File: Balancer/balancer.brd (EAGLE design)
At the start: 139.7 x 325.1 mm, 322 parts, among them Q1 BSS123W, Q10A SIR882DP-T1-GE3, Q10B SIS468DN-T1-GE3, Q11A SIR882DP-T1-GE3, Q11B SIS468DN-T1-GE3, Q12A SIR882DP-T1-GE3, Q12B SIS468DN-T1-GE3, Q1A8 SIR882DP-T1-GE3, Q1B8 SIS468DN-T1-GE3, Q2 BSS123W, Q3A SIR882DP-T1-GE3, Q3B SIS468DN-T1-GE3, Q4 MMBT3906LT1G, Q4A SIR882DP-T1-GE3, Q4B SIS468DN-T1-GE3, Q5 FDN5618P, Q5A SIR882DP-T1-GE3, Q5B SIS468DN-T1-GE3, Q6 CMPT3904E_TR_PBFREE, Q6A SIR882DP-T1-GE3, Q6B SIS468DN-T1-GE3, Q9A SIR882DP-T1-GE3, Q9B SIS468DN-T1-GE3, T10 750312504, T11 750312504, T12 750312504, T3 750312504, T4 750312504, T5 750312504, T6 750312504, T8 750312504, T9 750312504, U1 LTC3300ILXE-1PBF, U2 LTC3300ILXE-1PBF

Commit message: merged C8 and C6
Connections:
- removed net C8: C9A.2, C9B.2, C9G.2, D9C.A, D9E.P$2, D9E.P$3, R8K.1, R9J.1, RS9A.1
- net C6: now also C9A.2, C9B.2, C9G.2, D9C.A, D9E.P$2, D9E.P$3, R8K.1, R9J.1, RS9A.1
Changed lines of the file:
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@@
 <layers>
 <layer number="1" name="Top" color="4" fill="1" visible="yes" active="yes"/>
-<layer number="2" name="Route2" color="16" fill="1" visible="yes" active="yes"/>
+<layer number="2" name="Route2" color="16" fill="1" visible="no" active="yes"/>
 <layer number="3" name="Route3" color="17" fill="1" visible="no" active="no"/>
 <layer number="4" name="Route4" color="18" fill="1" visible="no" active="no"/>
@@
 <vertex x="95.758" y="258.191"/>
 </polygon>
+<contactref element="D9E" pad="P$2"/>
+<contactref element="D9E" pad="P$3"/>
+<contactref element="C9B" pad="2"/>
+<contactref element="C9A" pad="2"/>
+<contactref element="D9C" pad="A"/>
+<contactref element="C9G" pad="2"/>
+<contactref element="RS9A" pad="1"/>
+<contactref element="R9J" pad="1"/>
+<contactref element="R8K" pad="1"/>
 <wire x1="13.462" y1="244.21" x2="13.462" y2="240.4" width="0" layer="19" extent="1-1"/>
 <wire x1="17.907" y1="245.48" x2="13.462" y2="244.21" width="0" layer="19" extent="1-1"/>
@@
 <wire x1="30.75" y1="231.14" x2="26.46" y2="233.36" width="0" layer="19" extent="16-16"/>
 <wire x1="36.7" y1="232.41" x2="30.75" y2="231.14" width="0" layer="19" extent="16-16"/>
-<wire x1="42.418" y1="234.05" x2="36.7" y2="232.41" width="0" layer="19" extent="1-16"/>
+<wire x1="36.957" y1="233.669" x2="36.7" y2="232.41" width="0" layer="19" extent="1-16"/>
+<wire x1="39.116" y1="233.261" x2="36.957" y2="233.669" width="0" layer="19" extent="1-1"/>
+<wire x1="42.418" y1="234.05" x2="39.116" y2="233.261" width="0" layer="19" extent="1-1"/>
 <wire x1="15.24" y1="233.31" x2="13.462" y2="240.4" width="0" layer="19" extent="1-1"/>
 <wire x1="17.78" y1="233.31" x2="15.24" y2="233.31" width="0" layer="19" extent="1-1"/>
@@
 <wire x1="21.59" y1="256.67" x2="14.34" y2="252.73" width="0" layer="19" extent="1-1"/>
 <wire x1="44.32" y1="246.38" x2="42.418" y2="234.05" width="0" layer="19" extent="1-16"/>
+<wire x1="62.23" y1="223.84" x2="42.418" y2="234.05" width="0" layer="19" extent="1-1"/>
+<wire x1="67.158" y1="232.41" x2="62.23" y2="223.84" width="0" layer="19" extent="1-1"/>
+<wire x1="69.98" y1="236.22" x2="67.158" y2="232.41" width="0" layer="19" extent="1-1"/>
+<wire x1="69.98" y1="240.03" x2="69.98" y2="236.22" width="0" layer="19" extent="1-1"/>
+<wire x1="96.368" y1="234.95" x2="69.98" y2="236.22" width="0" layer="19" extent="1-1"/>
+<wire x1="97.92" y1="231.14" x2="96.368" y2="234.95" width="0" layer="19" extent="1-1"/>
+<wire x1="118.46" y1="218.118" x2="97.92" y2="231.14" width="0" layer="19" extent="1-16"/>
+<wire x1="120.3" y1="218.118" x2="118.46" y2="218.118" width="0" layer="19" extent="16-16"/>
+<wire x1="107.4928" y1="196.85" x2="118.46" y2="218.118" width="0" layer="19" extent="16-16"/>
+<wire x1="99.06" y1="191.77" x2="107.4928" y2="196.85" width="0" layer="19" extent="1-1"/>
+<wire x1="119.38" y1="181.46" x2="107.4928" y2="196.85" width="0" layer="19" extent="16-16"/>
+<wire x1="119.51" y1="170.18" x2="119.38" y2="181.46" width="0" layer="19" extent="16-16"/>
+<wire x1="98.933" y1="262.89" x2="96.368" y2="234.95" width="0" layer="19" extent="1-1"/>
 <wire x1="9.6" y1="200.7" x2="15.24" y2="233.31" width="0" layer="19" extent="1-1"/>
 <wire x1="9.6" y1="198.2" x2="9.6" y2="200.7" width="0" layer="19" extent="1-1"/>
@@
 <wire x1="18.796" y1="306.073" x2="21.59" y2="256.67" width="0" layer="19" extent="1-1"/>
 <wire x1="46.38" y1="306.832" x2="19.558" y2="308.61" width="0" layer="19" extent="1-1"/>
-<wire x1="96.368" y1="234.95" x2="44.32" y2="246.38" width="0" layer="19" extent="1-16"/>
-<wire x1="97.92" y1="231.14" x2="96.368" y2="234.95" width="0" layer="19" extent="1-1"/>
-<wire x1="98.933" y1="262.89" x2="96.368" y2="234.95" width="0" layer="19" extent="1-1"/>
-<wire x1="107.4928" y1="196.85" x2="97.92" y2="231.14" width="0" layer="19" extent="1-1"/>
-<wire x1="99.06" y1="191.77" x2="107.4928" y2="196.85" width="0" layer="19" extent="1-1"/>
-<wire x1="119.38" y1="181.46" x2="107.4928" y2="196.85" width="0" layer="19" extent="16-16"/>
-<wire x1="119.51" y1="170.18" x2="119.38" y2="181.46" width="0" layer="19" extent="16-16"/>
-<wire x1="109.54" y1="106.68" x2="119.51" y2="170.18" width="0" layer="19" extent="1-16"/>
+<wire x1="109.54" y1="109.22" x2="119.51" y2="170.18" width="0" layer="19" extent="1-16"/>
+<wire x1="109.54" y1="106.68" x2="109.54" y2="109.22" width="0" layer="19" extent="1-1"/>
 </signal>
 <signal name="C4">
@@
 <wire x1="39.116" y1="234.861" x2="62.23" y2="231.51" width="0" layer="19" extent="1-1"/>
 </signal>
-<signal name="C8">
-<contactref element="D9E" pad="P$2"/>
-<contactref element="D9E" pad="P$3"/>
-<contactref element="C9B" pad="2"/>
-<contactref element="C9A" pad="2"/>
-<contactref element="D9C" pad="A"/>
-<contactref element="C9G" pad="2"/>
-<contactref element="RS9A" pad="1"/>
-<contactref element="R9J" pad="1"/>
-<contactref element="R8K" pad="1"/>
-<wire x1="118.46" y1="218.118" x2="109.54" y2="109.22" width="0" layer="19" extent="1-16"/>
-<wire x1="120.3" y1="218.118" x2="118.46" y2="218.118" width="0" layer="19" extent="16-16"/>
-<wire x1="69.98" y1="236.22" x2="118.46" y2="218.118" width="0" layer="19" extent="1-16"/>
-<wire x1="69.98" y1="240.03" x2="69.98" y2="236.22" width="0" layer="19" extent="1-1"/>
-<wire x1="67.158" y1="232.41" x2="69.98" y2="236.22" width="0" layer="19" extent="1-1"/>
-<wire x1="62.23" y1="223.84" x2="67.158" y2="232.41" width="0" layer="19" extent="1-1"/>
-<wire x1="39.116" y1="233.261" x2="62.23" y2="223.84" width="0" layer="19" extent="1-1"/>
-<wire x1="36.957" y1="233.669" x2="39.116" y2="233.261" width="0" layer="19" extent="1-1"/>
-</signal>
 <signal name="N$75">

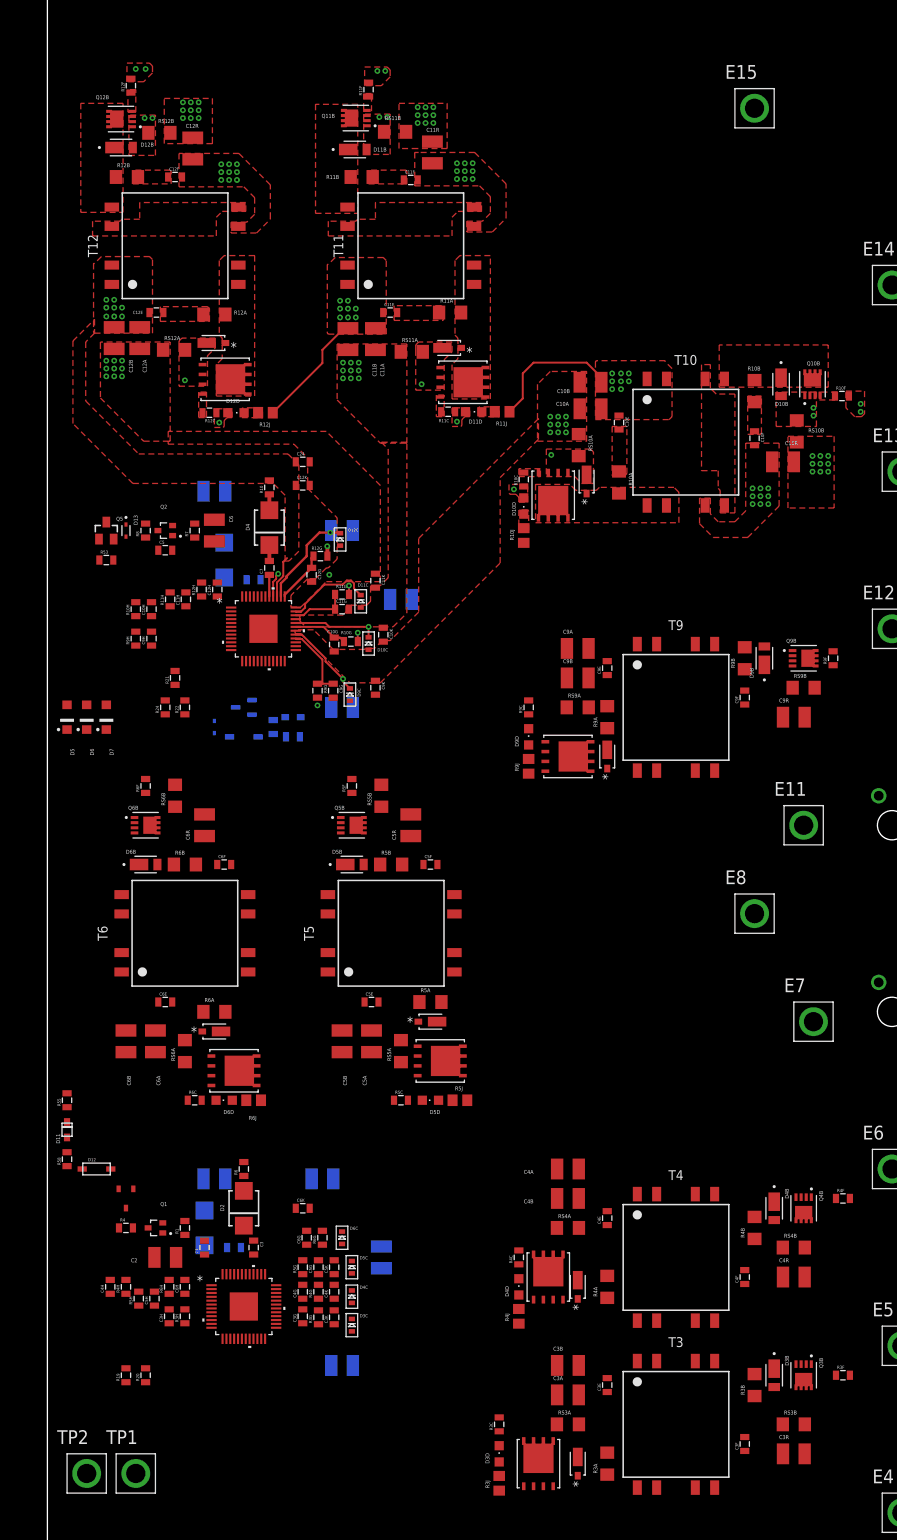
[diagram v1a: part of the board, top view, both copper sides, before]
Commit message: made more connections on L1 PCB
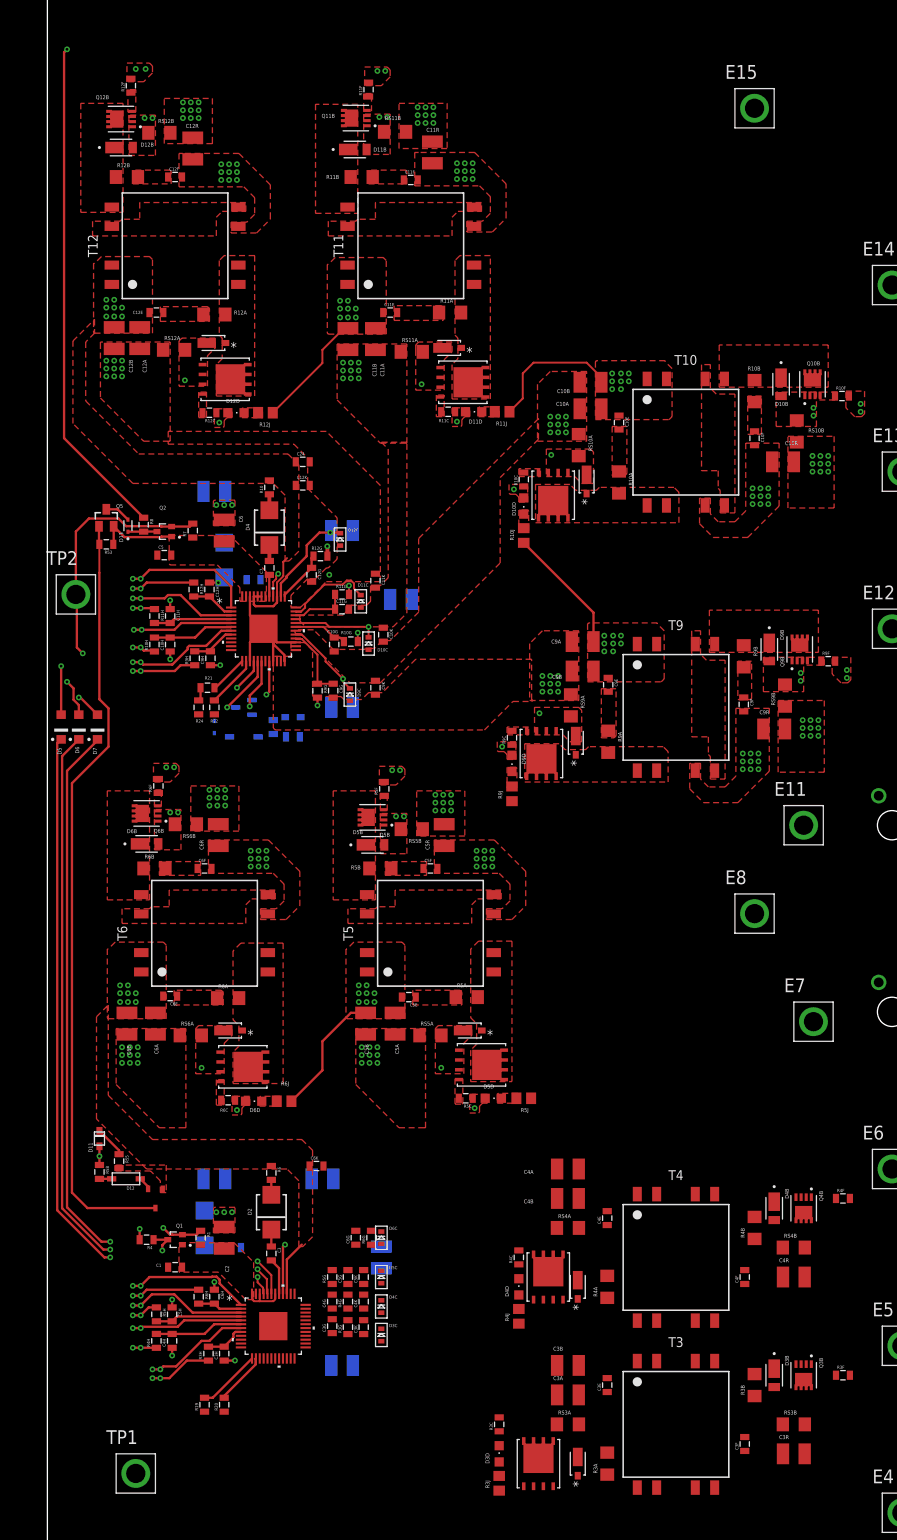
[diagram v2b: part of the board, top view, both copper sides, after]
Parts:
- moved TP2 113.7 mm to (3.68, 247.0)
- moved R19 10.9 mm to (20.3, 142.2)
- moved R20 10.9 mm to (22.9, 142.2)
- moved C4H 10.6 mm to (16.1, 150.5)
- moved R55 10.4 mm to (9.27, 173.7), turned to 270 degrees
- moved C3H 8.59 mm to (22.9, 148.8)
- moved R5C 8.39 mm to (54.1, 181.9), turned to 180 degrees
- moved R5J 8.26 mm to (61.6, 181.9), turned to 180 degrees
- moved D5D 8.13 mm to (57.7, 181.9), turned to 270 degrees
- moved C9H 8.03 mm to (21.1, 238.8)
- moved R9H 8.03 mm to (19.1, 238.8)
- moved C2 8.03 mm to (22.9, 163.8), turned to 90 degrees
- moved R4H 8.02 mm to (14.1, 150.5)
- moved C6G 6.35 mm to (39.9, 163.8)
- moved R6G 6.35 mm to (41.9, 163.8)
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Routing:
- net N$57: track 0.00 -> 100.3 mm
- net SDOI: track 0.00 -> 74.5 mm, vias 0 -> 2
- net SCKO: track 0.00 -> 73.7 mm, vias 0 -> 2
- net CSBO: track 0.00 -> 73.0 mm, vias 0 -> 2
- net TOP6_TS: track 0.00 -> 65.0 mm, vias 27 -> 37
- net WDTC: track 0.00 -> 37.0 mm, vias 0 -> 2
- net C6: track 0.00 -> 32.2 mm, vias 27 -> 60
- net C5: track 0.00 -> 18.9 mm, vias 0 -> 18
- net G12S: track 0.00 -> 16.8 mm, vias 2 -> 4
- net C9: track 0.00 -> 16.5 mm, vias 9 -> 17
- net G6S: track 0.00 -> 16.3 mm, vias 0 -> 4
- net G5S: track 0.00 -> 15.6 mm, vias 0 -> 4
- net G9S: track 0.00 -> 14.8 mm, vias 0 -> 4
- net G4S: track 0.00 -> 14.4 mm, vias 0 -> 2
- net G11S: track 0.00 -> 14.0 mm, vias 2 -> 4
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- added copper zone on layer 1, net BOT6_TS
- added copper zone on layer 1, net C4
- added copper zone on layer 1, net C5
- added copper zone on layer 1, net G5P
- added copper zone on layer 1, net G5S
- added copper zone on layer 1, net G6P
- added copper zone on layer 1, net G6S
- added copper zone on layer 1, net G9P
- added copper zone on layer 1, net G9S
- added copper zone on layer 1, net N$13
- added copper zone on layer 1, net N$34
- added copper zone on layer 1, net N$37
- added copper zone on layer 1, net N$40
- added copper zone on layer 1, net N$43
- added copper zone on layer 1, net N$45
- added copper zone on layer 1, net N$47
- added copper zone on layer 1, net N$48
- added copper zone on layer 1, net N$49
- added copper zone on layer 1, net N$51
- added copper zone on layer 1, net N$52
- added copper zone on layer 1, net N$54
- added copper zone on layer 1, net N$56
- added copper zone on layer 1, net N$59
- added copper zone on layer 1, net N$61
- added copper zone on layer 1, net N$63
- added copper zone on layer 1, net N$64
- added copper zone on layer 1, net N$65
- added copper zone on layer 1, net N$67
- added copper zone on layer 1, net N$68
- added copper zone on layer 1, net N$70
- added copper zone on layer 1, net N$72
- added copper zone on layer 1, net N$75
- added copper zone on layer 1, net N$77
- added copper zone on layer 1, net N$79
- added copper zone on layer 1, net N$80
- added copper zone on layer 1, net N$81
- added copper zone on layer 1, net N$83
- added copper zone on layer 1, net N$84
- added copper zone on layer 1, net N$86
- added copper zone on layer 1, net V-
- added copper zone on layer 1, net VREG
- added copper zone on layer 1, net VREG2

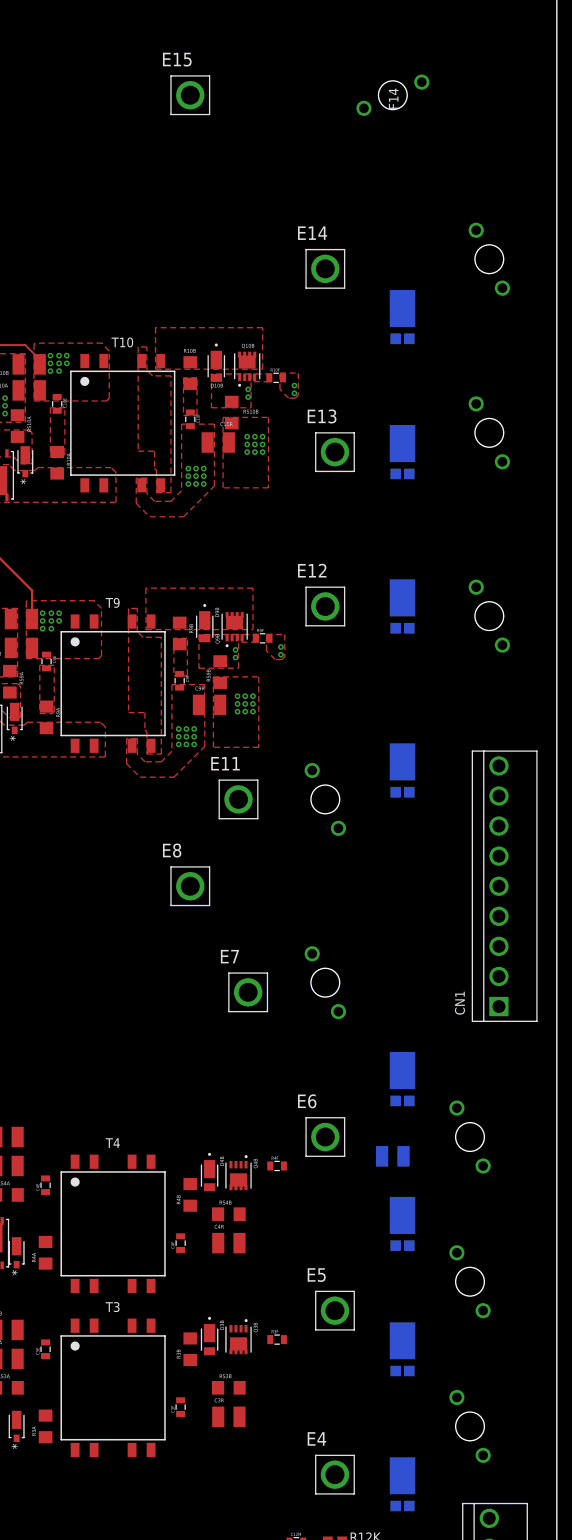
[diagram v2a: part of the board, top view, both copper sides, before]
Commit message: Finished L2 and L3 Copper Pours
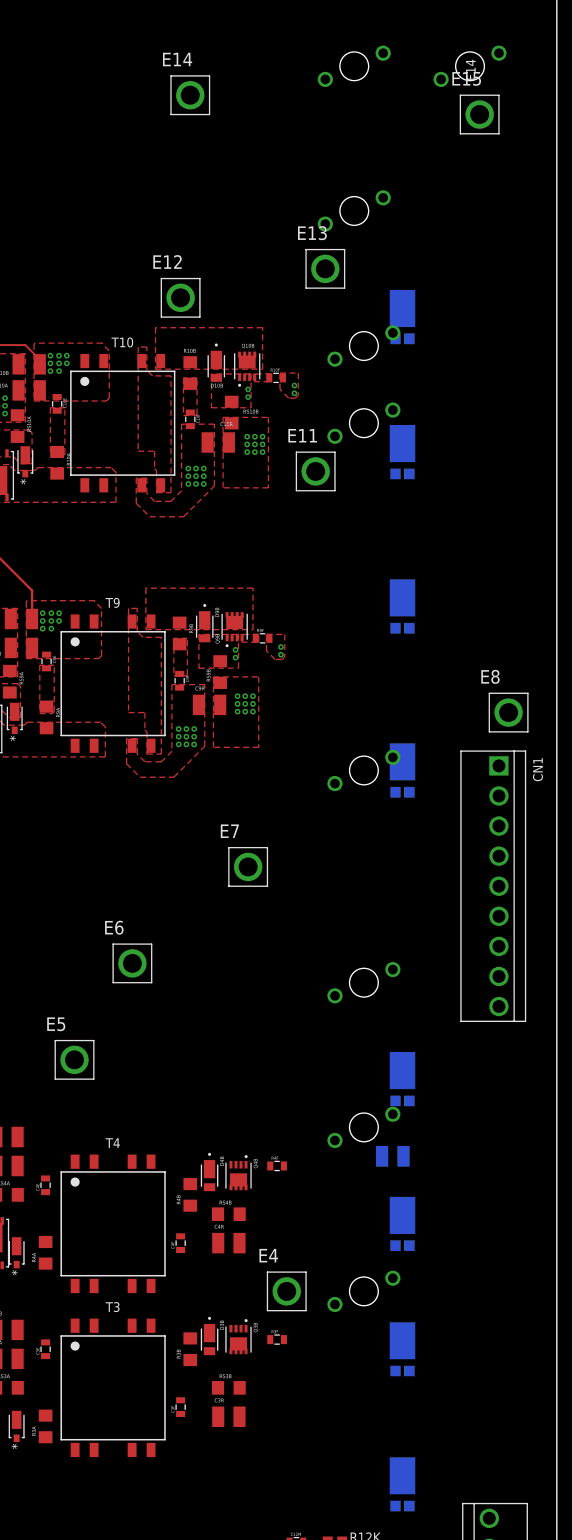
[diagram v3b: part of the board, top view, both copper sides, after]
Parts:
- moved F9 49.8 mm to (114.3, 266.7), turned to 90 degrees
- moved E8 47.7 mm to (133.3, 228.6)
- moved E5 47.6 mm to (76.2, 182.9)
- moved E12 44.9 mm to (90.2, 283.2)
- moved E11 44.4 mm to (108.0, 260.4)
- moved F10 39.2 mm to (114.3, 276.9), turned to 270 degrees
- moved E15 38.2 mm to (129.5, 307.3)
- moved F11 34.2 mm to (113.0, 294.6), turned to 90 degrees
- moved E6 34.2 mm to (83.8, 195.6)
- moved F12 31.0 mm to (113.0, 313.7), turned to 270 degrees
- moved E14 29.0 mm to (91.4, 309.9)
- moved F6 28.4 mm to (114.3, 221.0), turned to 270 degrees
- moved E4 25.0 mm to (104.1, 152.4)
- moved F4 24.7 mm to (114.3, 174.0), turned to 270 degrees
- moved F5 24.7 mm to (114.3, 193.0), turned to 270 degrees
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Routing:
- added copper zone on layer 2, net C10
- added copper zone on layer 2, net C11
- added copper zone on layer 2, net C12
- added copper zone on layer 2, net C3
- added copper zone on layer 2, net C4
- added copper zone on layer 2, net C5
- added copper zone on layer 15, net C6
- added copper zone on layer 2, net C6
- added copper zone on layer 2, net C9
- added copper zone on layer 15, net V-
- removed copper zone on layer 2, net L2-COPPER-POUR-1
- removed copper zone on layer 2, net L2-COPPER-POUR-2
